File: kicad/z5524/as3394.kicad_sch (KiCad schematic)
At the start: 36 parts, among them U11 DG442xY, U15 AS3394, U16 TL074

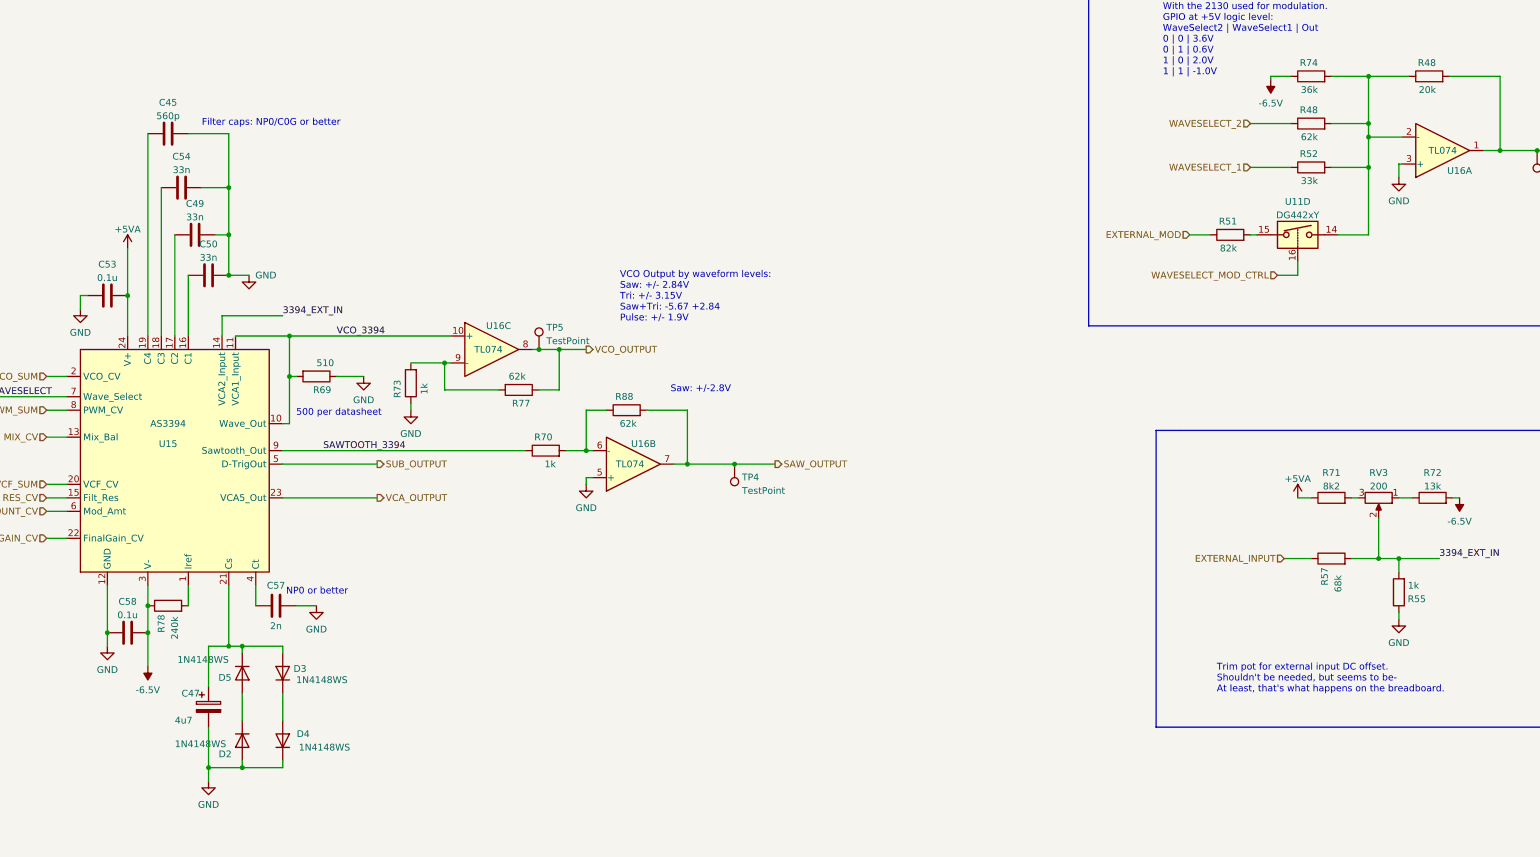
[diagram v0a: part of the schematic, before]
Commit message: reannotate geographically
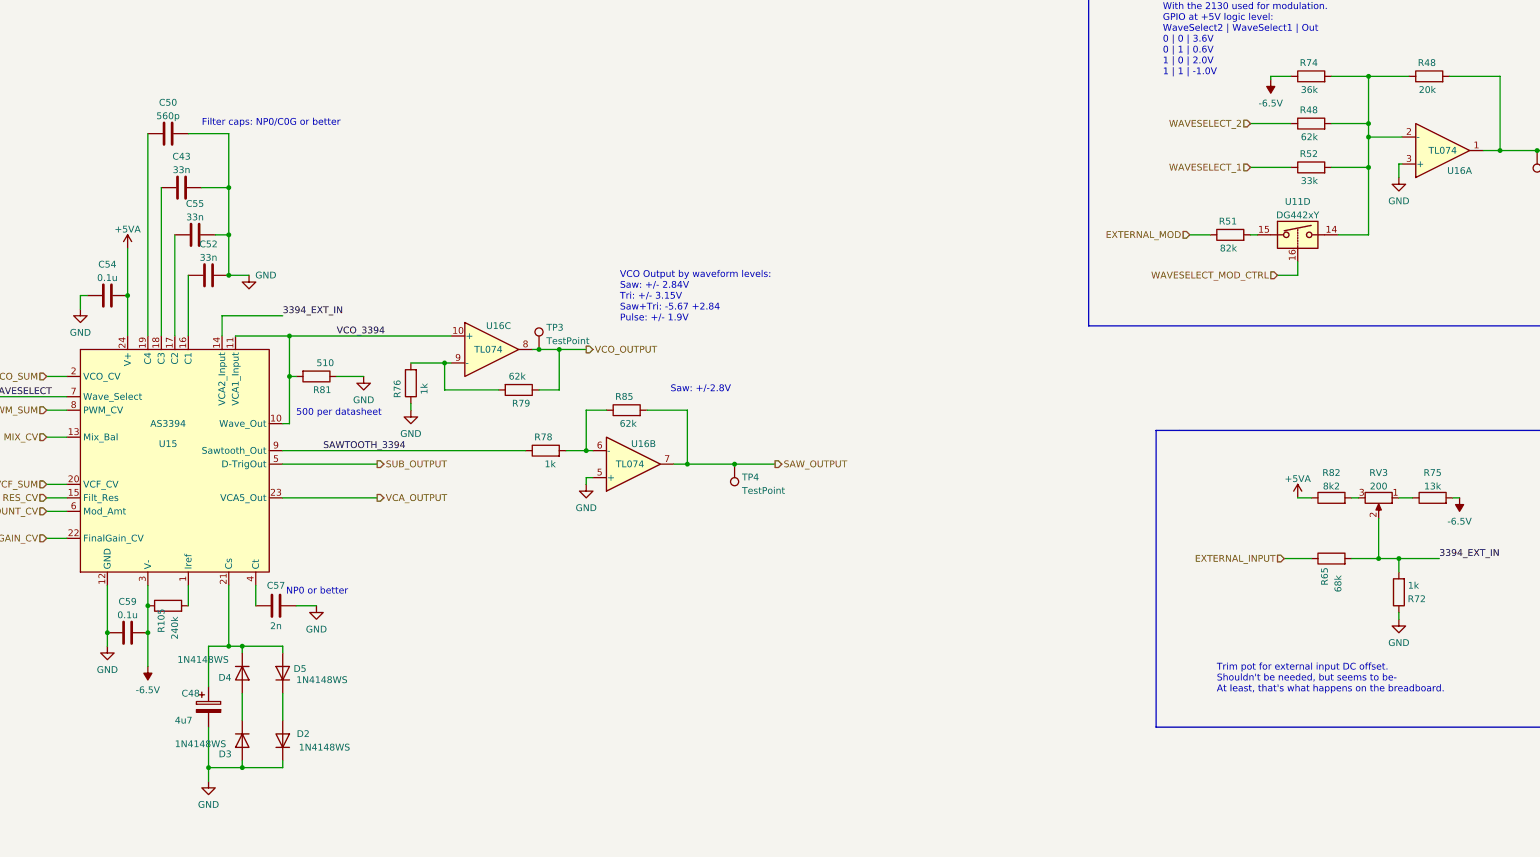
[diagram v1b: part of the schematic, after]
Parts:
- renumbered C54 to C43, C47 to C48, C45 to C50, C50 to C52, C53 to C54, C49 to C55, C58 to C59, D4 to D2, D2 to D3, D5 to D4, D3 to D5, R78 to R105, R57 to R65, R55 to R72, R72 to R75, R73 to R76, R70 to R78, R77 to R79, R69 to R81, R71 to R82, R88 to R85, TP5 to TP3

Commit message: minor rework
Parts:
- R48: LCSC (none) -> C4184
- R48: LCSC (none) -> C23221
- R51: LCSC (none) -> C23254
- R52: LCSC (none) -> C4216
- R74: LCSC (none) -> C23147
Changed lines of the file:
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@@
       (effects (font (size 1.27 1.27)) hide)
     )
-    (property "LCSC" "" (at 355.6 36.195 0)
+    (property "LCSC" "C4184" (at 355.6 36.195 0)
       (effects (font (size 1.27 1.27)) hide)
     )
@@
       (effects (font (size 1.27 1.27)) hide)
     )
-    (property "LCSC" "" (at 333.375 45.085 0)
+    (property "LCSC" "C23221" (at 333.375 45.085 0)
       (effects (font (size 1.27 1.27)) hide)
     )
@@
       (effects (font (size 1.27 1.27)) hide)
     )
-    (property "LCSC" "" (at 333.375 36.195 0)
+    (property "LCSC" "C23147" (at 333.375 36.195 0)
       (effects (font (size 1.27 1.27)) hide)
     )
@@
       (effects (font (size 1.27 1.27)) hide)
     )
-    (property "LCSC" "" (at 318.135 66.04 0)
+    (property "LCSC" "C23254" (at 318.135 66.04 0)
       (effects (font (size 1.27 1.27)) hide)
     )
@@
       (effects (font (size 1.27 1.27)) hide)
     )
-    (property "LCSC" "" (at 333.375 53.34 0)
-      (effects (font (size 1.27 1.27)) hide)
-    )
+    (property "LCSC" "C4216" (at 333.375 53.34 0)
+      (effects (font (size 1.27 1.27)) hide)
+    )

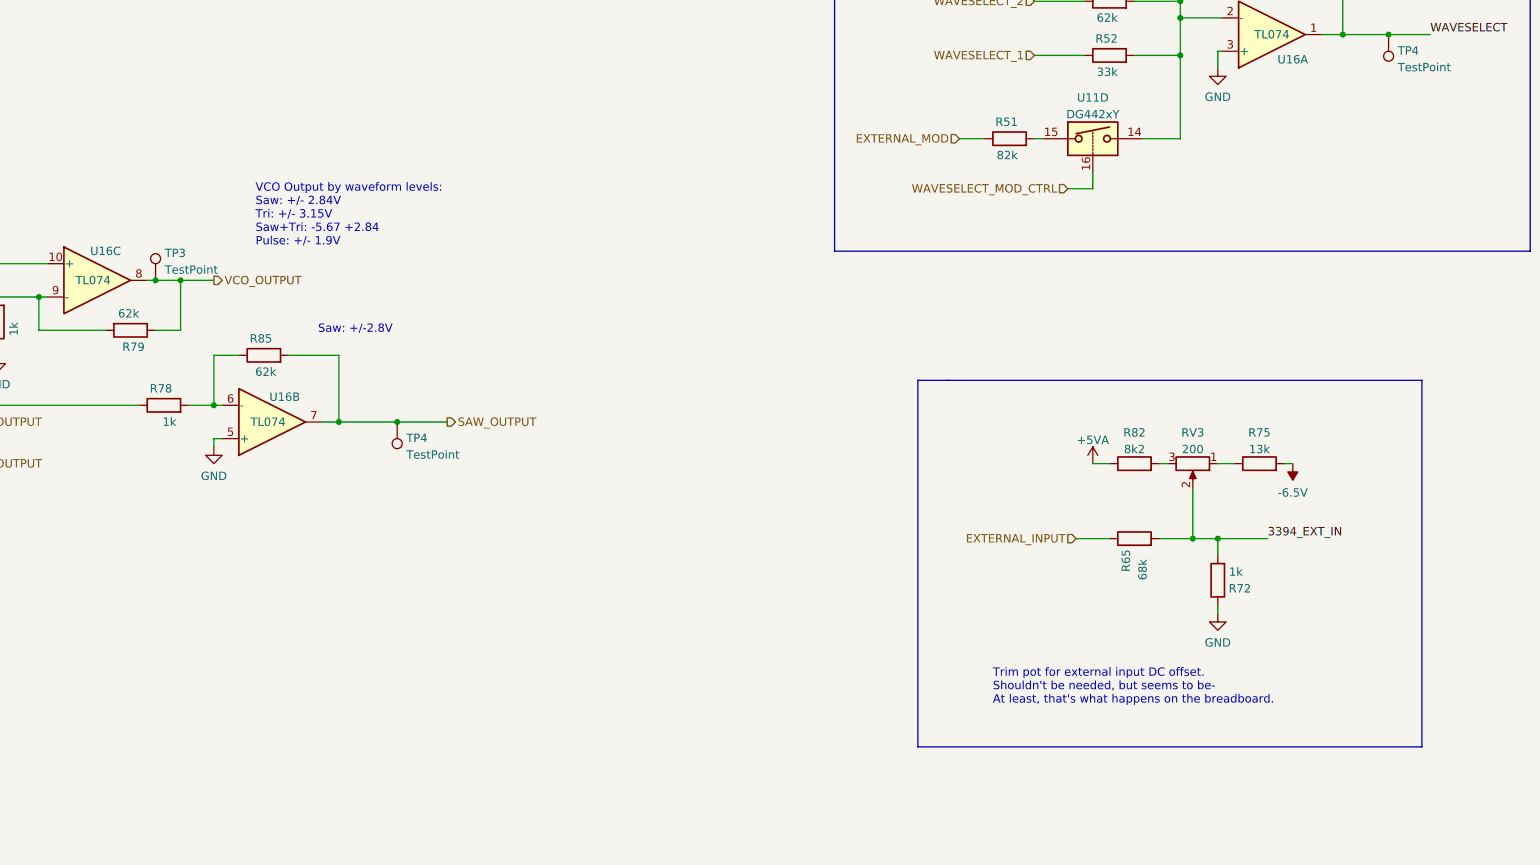
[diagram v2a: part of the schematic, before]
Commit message: updated 3394 --> 2130 FM to much deeper.  Started addressing PWM range for increased modulation
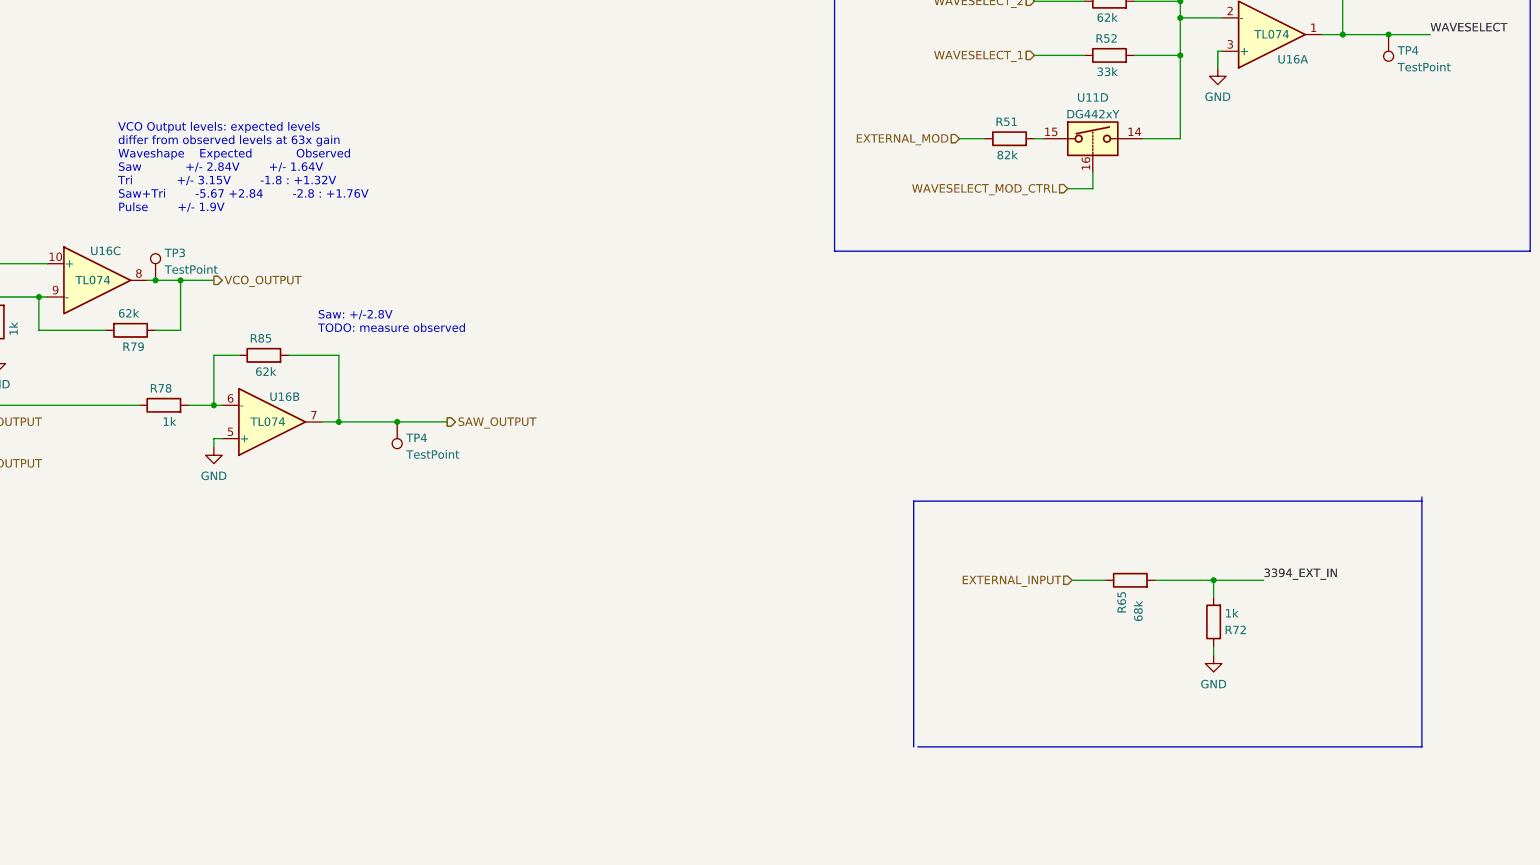
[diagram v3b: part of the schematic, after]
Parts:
- removed R75: 13k, Resistor_SMD:R_0603_1608Metric, symbol Device:R
- removed R82: 8k2, Resistor_SMD:R_0603_1608Metric, symbol Device:R
- removed RV3: 200, Potentiometer_THT:Potentiometer_Bourns_3296W_Vertical, symbol Device:R_Potentiometer
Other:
- note added: "Saw: +/-2.8V TODO: measure observed"
- note added: "VCO Output levels: expected levels differ from observed levels at 63x gain Waveshape Expected Observed Saw +/- 2.84V +/- 1.64V Tri +/- 3.15V -1.8 : +1.32V Saw+Tri -5.67 +2.84 -2.8 : +1.76V Pulse +/- 1.9V"
- note removed: "Saw: +/-2.8V"
- note removed: "Trim pot for external input DC offset. Shouldn't be needed, but seems to be- At least, that's what happens on the breadboard."
- note removed: "VCO Output by waveform levels: Saw: +/- 2.84V Tri: +/- 3.15V Saw+Tri: -5.67 +2.84 Pulse: +/- 1.9V"
- moved on the sheet: R65, R72

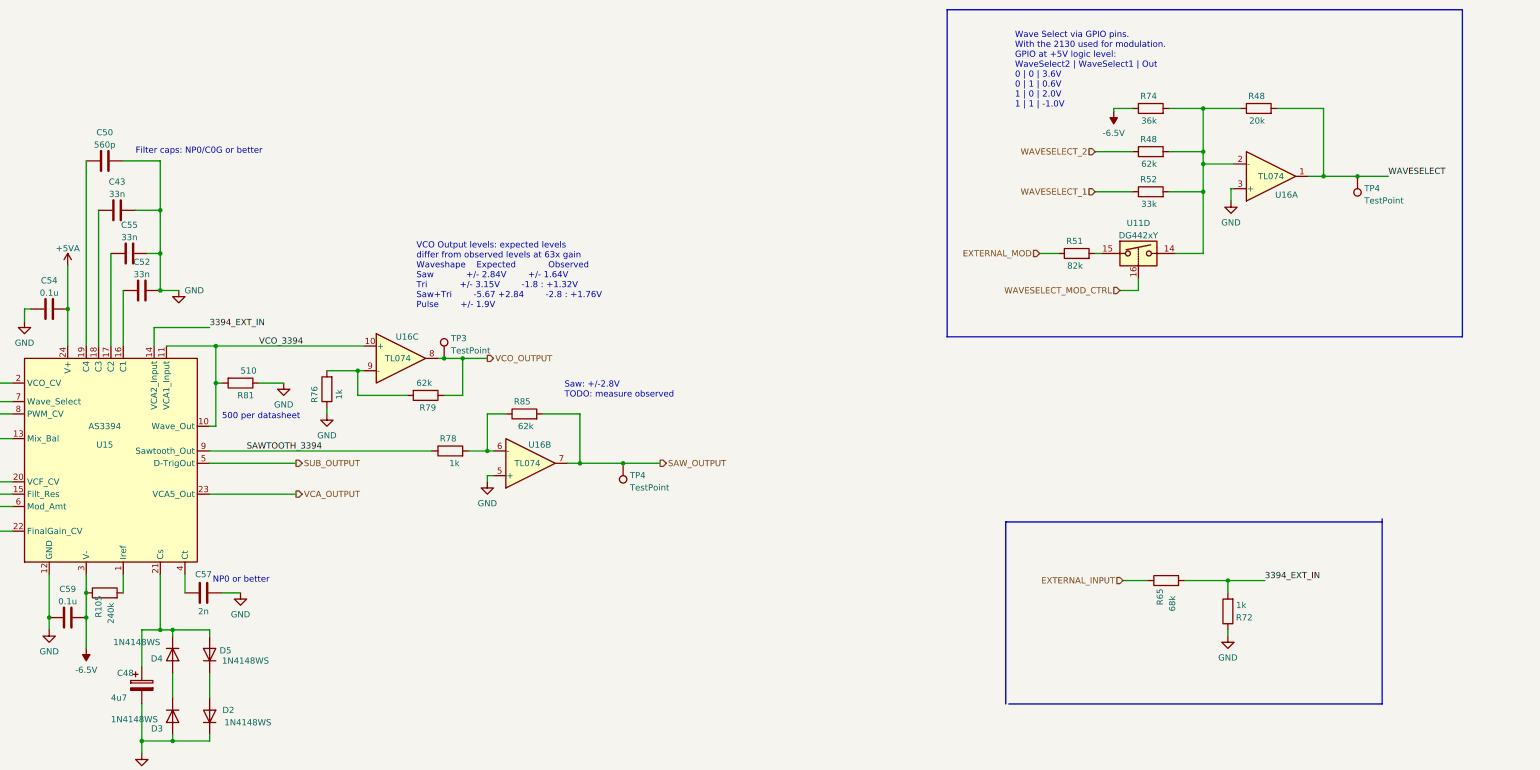
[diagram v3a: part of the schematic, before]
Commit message: fix 2130 exp pitch input and save an opamp
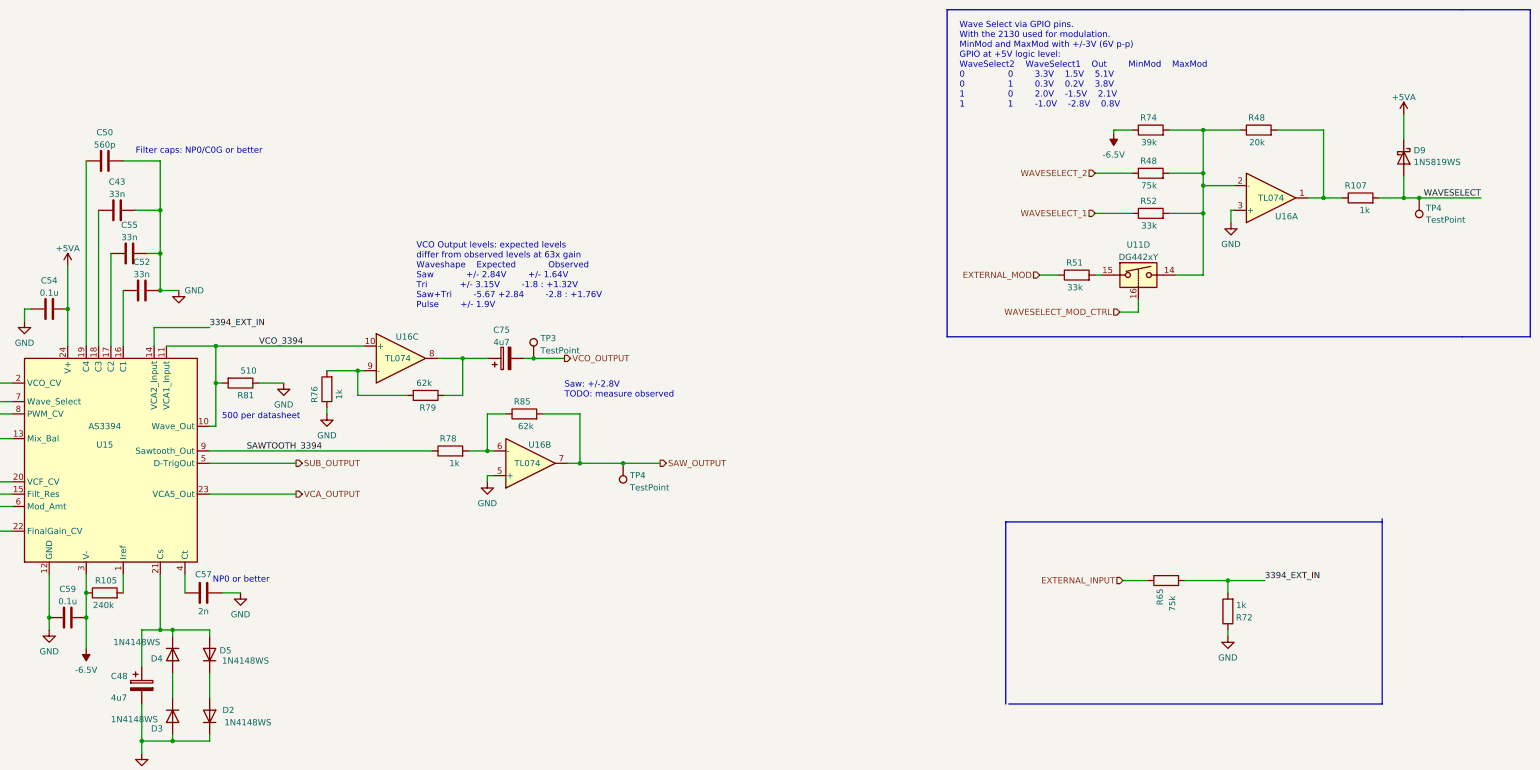
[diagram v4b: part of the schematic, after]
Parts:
- added C75: 4u7, Capacitor_THT:CP_Radial_D4.0mm_P2.00mm, symbol Device:C_Polarized
- added D9: 1N5819WS, Diode_SMD:D_SOD-323, symbol Diode:1N5819WS
- added R107: 1k, Resistor_SMD:R_0603_1608Metric, symbol Device:R
- R48: value 62k -> 75k; LCSC C23221 -> (none)
- R51: value 82k -> 33k; LCSC C23254 -> (none)
- R65: value 68k -> 75k; LCSC C23231 -> (none)
- R74: value 36k -> 39k; LCSC C23147 -> (none)
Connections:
- net +5VA: now also D9.1 (K)
- net VCO_OUTPUT: now also C75.2; no longer R79.1, U16.8
- net WAVESELECT: now also D9.2 (A), R107.2; no longer R48.2, U16.1
- new net: R107.1, R48.2, U16.1
- new net: C75.1, R79.1, U16.8
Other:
- note added: "Wave Select via GPIO pins. With the 2130 used for modulation. MinMod and MaxMod with +/-3V (6V p-p) GPIO at +5V logic level: WaveSelect2 WaveSelect1 Out MinMod MaxMod 0 0 3.3V 1.5V 5.1V 0 1 0.3V 0.2V 3.8V 1 0 2.0V -1.5V 2.1V 1 1 -1.0V -2.8V 0.8V"
- note removed: "Wave Select via GPIO pins. With the 2130 used for modulation. GPIO at +5V logic level: WaveSelect2 | WaveSelect1 | Out 0 | 0 | 3.6V 0 | 1 | 0.6V 1 | 0 | 2.0V 1 | 1 | -1.0V"
- moved on the sheet: R48, R51, R52, R74, TP3, TP4, U11D, U16A
